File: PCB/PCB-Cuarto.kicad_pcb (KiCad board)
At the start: 4 copper layers, 90 x 100 mm, 80 parts, among them IC100 AP63203WU-7, J100 2604-3102, J200 2171790001, J201 2086-1104, J300 2086-1102, J301 jumper, J302 2086-1104, J303 2086-1104, Q100 CSD19537Q3, Q101 BSS138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

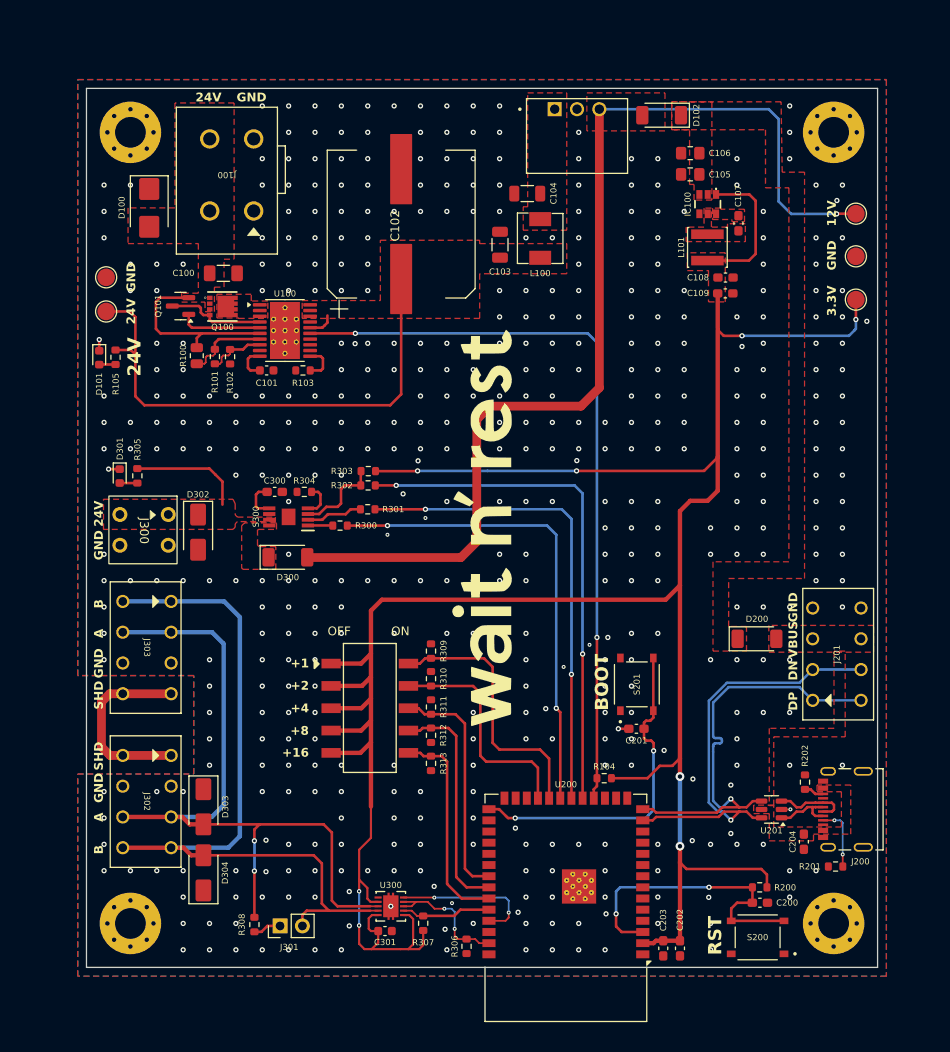
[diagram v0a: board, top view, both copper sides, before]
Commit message: Change Placement
Se ha cambiado el placement total para obtener una mejor posicion de conexion de los perifericos
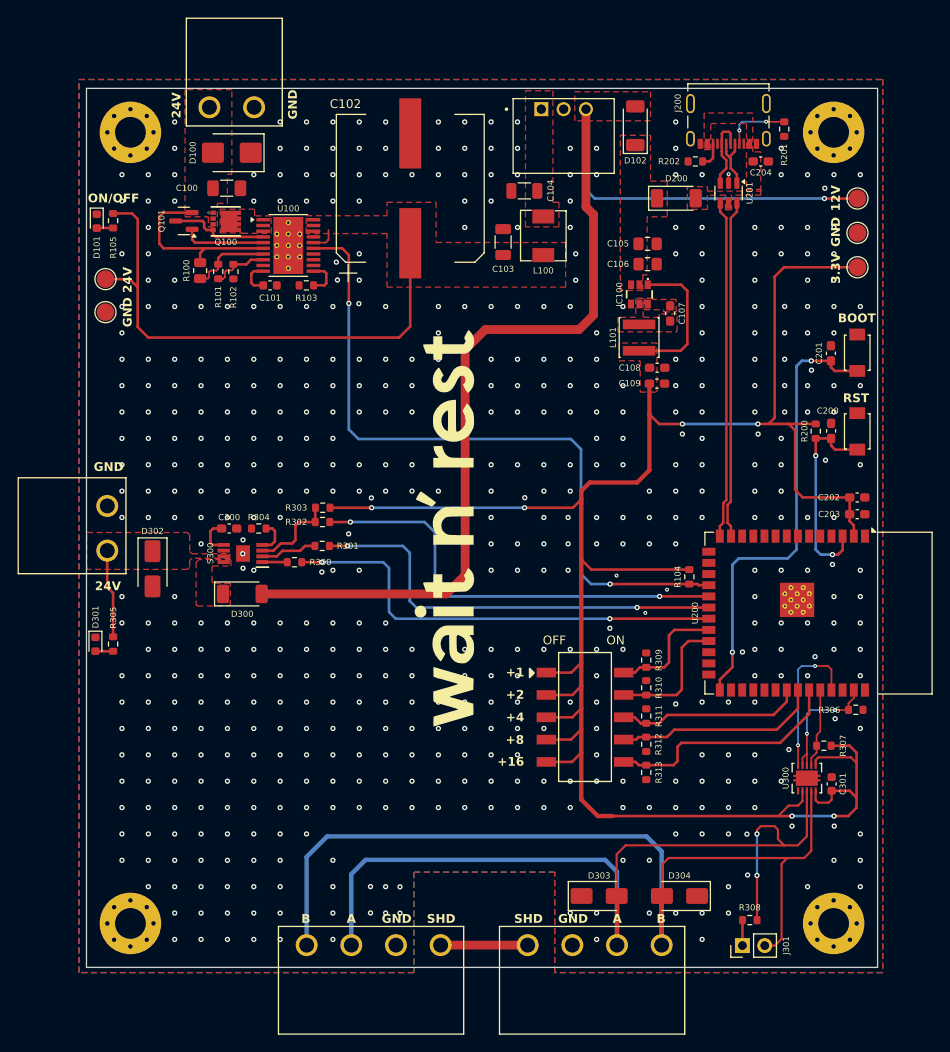
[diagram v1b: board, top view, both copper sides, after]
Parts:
- removed J201: 2086-1104, 2086-1104-THT:2086-1104-THT
- J100: value 2604-3102 -> 282814-2; footprint 2604-3102:2604-3102 -> 282814-2:282814-2
- J300: value 2086-1102 -> 282814-2; footprint 2086-1102-THT:2086-1102-THT -> 282814-2:282814-2
- J302, J303: value 2086-1104 -> 282814-4; footprint 2086-1104-THT:2086-1104-THT -> 282814-4:282814-4
- S200, S201: value TS-1187A-B-A-B -> TS-1088-AR02016; footprint TS-1187A-B-A-B:TS-1187A-B-A-B -> TS-1088-AR02016:TS-1088-AR02016
- moved R201 84.1 mm to (184.4, 52.6), turned to -90 degrees
- moved J200 80.4 mm to (178.0, 50.9), turned to 180 degrees
- moved C204 77.5 mm to (181.7, 56.3), turned to 0 degrees
- moved R202 71.7 mm to (174.3, 56.3), turned to 180 degrees
- moved U201 70.3 mm to (178.0, 59.9), turned to -90 degrees
- moved S200 58.7 mm to (192.7, 87.0), turned to -90 degrees
- moved R308 56.4 mm to (180.5, 142.6), turned to 0 degrees
- moved J303 56.3 mm to (155.2, 145.5), turned to 0 degrees
- moved C202 55.1 mm to (192.7, 94.5), turned to 0 degrees
- moved C200 54.3 mm to (189.7, 87.0), turned to 90 degrees
- moved D304 54.2 mm to (172.5, 139.9), turned to 180 degrees
- moved C203 54.1 mm to (192.7, 96.4), turned to 0 degrees
- moved C301 53.5 mm to (189.8, 127.1), turned to 90 degrees
- moved J301 52.6 mm to (179.6, 145.5)
- moved R200 52.3 mm to (188.0, 87.0), turned to -90 degrees
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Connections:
- J100 pad 2: GND -> /POWER/INPUT
- J300 pad 1: Net-(D302-A1) -> GND
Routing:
- net +3.3V: track 301.4 -> 259.0 mm, vias 8 -> 6
- net /PERIPHERALS/B: track 86.5 -> 108.1 mm
- net /ID1: track 30.5 -> 13.5 mm
- net /PERIPHERALS/A: track 85.5 -> 101.0 mm
- net /MCU/BOOT: track 38.3 -> 51.8 mm
- net /PERIPHERALS/SHIELD: track 21.7 -> 9.91 mm
- net /MCU/EN: track 34.8 -> 23.5 mm
- net /ID2: track 26.2 -> 15.0 mm
- net /MCU/USB_N: track 49.3 -> 38.5 mm, vias 1 -> 0
- net /MCU/USB_P: track 49.2 -> 38.5 mm, vias 1 -> 0
- net +12V: track 120.7 -> 130.2 mm
- net /MCU/DOOR_FAULT: track 58.6 -> 50.4 mm
- net /ID3: track 26.7 -> 21.2 mm
- net /MCU/DOOR_DIAG_EN: track 54.6 -> 49.3 mm
- net /MCU/FLT: track 85.1 -> 80.8 mm
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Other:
- board text added: "ON/OFF"
- board text removed: "DN"
- board text removed: "DP"
- board text removed: "VBUS"
